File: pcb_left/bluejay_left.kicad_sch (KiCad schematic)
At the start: 0 parts

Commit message: Start building left pcb
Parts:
- added C1, C2: 22p, symbol Device:C_Small
- added U1: ATmega328P-PU, Package_DIP_AKL:DIP-28_W7.62mm_Socket, symbol BlueJaySymbolLibrary:ATmega328P-PU
- added Y1: 16MHz, symbol BlueJaySymbolLibrary:Device_Crystal_Small
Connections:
- new net: C1.1, U1.9 (XTAL1/PB6), Y1.2
- new net: C2.1, U1.10 (XTAL2/PB7), Y1.1
- new net GND: C1.2, C2.2, U1.22 (GND), U1.8 (GND)
- new net VCC: U1.20 (AVCC), U1.7 (VCC)
- no-connect marks 0 -> 1
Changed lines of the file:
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@@
 (kicad_sch (version 20211123) (generator eeschema)
   (paper "USLetter")
+  (junction (at 34.29 114.3) (diameter 0) (color 0 0 0 0)
+  )
+  (junction (at 55.88 143.51) (diameter 0) (color 0 0 0 0)
+  )
+  (junction (at 55.88 138.43) (diameter 0) (color 0 0 0 0)
+  )
+  (junction (at 73.66 146.05) (diameter 0) (color 0 0 0 0)
+  )
+  (no_connect (at 19.05 124.46))
+  (wire (pts (xy 55.88 138.43) (xy 55.88 135.89))
+    (stroke (width 0) (type default) (color 0 0 0 0))
+  )
+  (wire (pts (xy 49.53 138.43) (xy 49.53 139.7))
+    (stroke (width 0) (type default) (color 0 0 0 0))
+  )
+  (wire (pts (xy 73.66 135.89) (xy 73.66 146.05))
+    (stroke (width 0) (type default) (color 0 0 0 0))
+  )
+  (wire (pts (xy 36.83 114.3) (xy 34.29 114.3))
+    (stroke (width 0) (type default) (color 0 0 0 0))
+  )
+  (wire (pts (xy 67.31 135.89) (xy 73.66 135.89))
+    (stroke (width 0) (type default) (color 0 0 0 0))
+  )
+  (wire (pts (xy 55.88 138.43) (xy 49.53 138.43))
+    (stroke (width 0) (type default) (color 0 0 0 0))
+  )
+  (wire (pts (xy 34.29 110.49) (xy 34.29 114.3))
+    (stroke (width 0) (type default) (color 0 0 0 0))
+  )
+  (wire (pts (xy 55.88 143.51) (xy 49.53 143.51))
+    (stroke (width 0) (type default) (color 0 0 0 0))
+  )
+  (wire (pts (xy 36.83 116.84) (xy 36.83 114.3))
+    (stroke (width 0) (type default) (color 0 0 0 0))
+  )
+  (wire (pts (xy 34.29 193.04) (xy 34.29 196.85))
+    (stroke (width 0) (type default) (color 0 0 0 0))
+  )
+  (wire (pts (xy 55.88 135.89) (xy 62.23 135.89))
+    (stroke (width 0) (type default) (color 0 0 0 0))
+  )
+  (wire (pts (xy 34.29 114.3) (xy 34.29 116.84))
+    (stroke (width 0) (type default) (color 0 0 0 0))
+  )
+  (wire (pts (xy 49.53 143.51) (xy 49.53 142.24))
+    (stroke (width 0) (type default) (color 0 0 0 0))
+  )
+  (wire (pts (xy 55.88 143.51) (xy 55.88 146.05))
+    (stroke (width 0) (type default) (color 0 0 0 0))
+  )
+  (wire (pts (xy 67.31 146.05) (xy 73.66 146.05))
+    (stroke (width 0) (type default) (color 0 0 0 0))
+  )
+  (wire (pts (xy 55.88 146.05) (xy 62.23 146.05))
+    (stroke (width 0) (type default) (color 0 0 0 0))
+  )
+  (symbol (lib_id "power:GND") (at 34.29 196.85 0) (unit 1)
+    (in_bom yes) (on_board yes) (fields_autoplaced)
+    (property "Reference" "#PWR?" (id 0) (at 34.29 203.2 0)
+      (effects (font (size 1.27 1.27)) hide)
+    )
+    (property "Value" "GND" (id 1) (at 34.29 201.93 0))
+    (property "Footprint" "" (id 2) (at 34.29 196.85 0)
+      (effects (font (size 1.27 1.27)) hide)
+    )
+    (property "Datasheet" "" (id 3) (at 34.29 196.85 0)
+      (effects (font (size 1.27 1.27)) hide)
+    )
+    (pin "1")
+  )
+  (symbol (lib_id "Device:C_Small") (at 64.77 135.89 90) (unit 1)
+    (in_bom yes) (on_board yes) (fields_autoplaced)
+    (property "Reference" "C1" (id 0) (at 64.7763 129.54 90))
+    (property "Value" "22p" (id 1) (at 64.7763 132.08 90))
+    (property "Footprint" "" (id 2) (at 64.77 135.89 0)
+      (effects (font (size 1.27 1.27)) hide)
+    )
+    (property "Datasheet" "~" (id 3) (at 64.77 135.89 0)
+      (effects (font (size 1.27 1.27)) hide)
+    )
+    (pin "1")
+    (pin "2")
+  )
+  (symbol (lib_id "Device:C_Small") (at 64.77 146.05 90) (unit 1)
+    (in_bom yes) (on_board yes)
+    (property "Reference" "C2" (id 0) (at 64.77 149.86 90))
+    (property "Value" "22p" (id 1) (at 64.77 152.4 90))
+    (property "Footprint" "" (id 2) (at 64.77 146.05 0)
+      (effects (font (size 1.27 1.27)) hide)
+    )
+    (property "Datasheet" "~" (id 3) (at 64.77 146.05 0)
+      (effects (font (size 1.27 1.27)) hide)
+    )
+    (pin "1")
+    (pin "2")
+  )
+  (symbol (lib_id "BlueJaySymbolLibrary:Device_Crystal_Small") (at 55.88 140.97 90) (unit 1)
+    (in_bom yes) (on_board yes)
+    (property "Reference" "Y1" (id 0) (at 57.15 138.43 90)
+      (effects (font (size 1.27 1.27)) (justify right))
+    )
+    (property "Value" "16MHz" (id 1) (at 55.88 144.78 90)
+      (effects (font (size 1.27 1.27)) (justify right))
+    )
+    (property "Footprint" "" (id 2) (at 55.88 140.97 0)
+      (effects (font (size 1.27 1.27)) hide)
+    )
+    (property "Datasheet" "" (id 3) (at 55.88 140.97 0)
+      (effects (font (size 1.27 1.27)) hide)
+    )
+    (pin "1")
+    (pin "2")
+  )
+  (symbol (lib_id "power:VCC") (at 34.29 110.49 0) (unit 1)
+    (in_bom yes) (on_board yes) (fields_autoplaced)
+    (property "Reference" "#PWR?" (id 0) (at 34.29 114.3 0)
+      (effects (font (size 1.27 1.27)) hide)
+    )
+    (property "Value" "VCC" (id 1) (at 34.29 105.41 0))
+    (property "Footprint" "" (id 2) (at 34.29 110.49 0)
+      (effects (font (size 1.27 1.27)) hide)
+    )
+    (property "Datasheet" "" (id 3) (at 34.29 110.49 0)
+      (effects (font (size 1.27 1.27)) hide)
+    )
+    (pin "1")
+  )
+  (symbol (lib_id "power:GND") (at 73.66 146.05 0) (unit 1)
+    (in_bom yes) (on_board yes) (fields_autoplaced)
+    (property "Reference" "#PWR?" (id 0) (at 73.66 152.4 0)
+      (effects (font (size 1.27 1.27)) hide)
+    )
+    (property "Value" "GND" (id 1) (at 73.66 151.13 0))
+    (property "Footprint" "" (id 2) (at 73.66 146.05 0)
+      (effects (font (size 1.27 1.27)) hide)
+    )
+    (property "Datasheet" "" (id 3) (at 73.66 146.05 0)
+      (effects (font (size 1.27 1.27)) hide)
+    )
+    (pin "1")
+  )
+  (symbol (lib_id "BlueJaySymbolLibrary:ATmega328P-PU") (at 34.29 154.94 0) (unit 1)
+    (in_bom yes) (on_board yes)
+    (property "Reference" "U1" (id 0) (at 21.59 114.3 0))
+    (property "Value" "ATmega328P-PU" (id 1) (at 21.59 116.84 0))
+    (property "Footprint" "Package_DIP_AKL:DIP-28_W7.62mm_Socket" (id 2) (at 34.29 154.94 0)
+      (effects (font (size 1.27 1.27) italic) hide)
+    )
+    (property "Datasheet" "" (id 3) (at 34.29 154.94 0)
+      (effects (font (size 1.27 1.27)) hide)
+    )
+    (pin "1")
+    (pin "10")
+    (pin "11")
+    (pin "12")
+    (pin "13")
+    (pin "14")
+    (pin "15")
+    (pin "16")
+    (pin "17")
+    (pin "18")
+    (pin "19")
+    (pin "2")
+    (pin "20")
+    (pin "21")
+    (pin "22")
+    (pin "23")
+    (pin "24")
+    (pin "25")
+    (pin "26")
+    (pin "27")
+    (pin "28")
+    (pin "3")
+    (pin "4")
+    (pin "5")
+    (pin "6")
+    (pin "7")
+    (pin "8")
+    (pin "9")
+  )
   (sheet_instances
     (path "/" (page "1"))
   )
+  (symbol_instances
+    (path "/35c4581b-ad58-4c6a-b9b5-a7da8d3ffce0"
+      (reference "#PWR?") (unit 1) (value "GND") (footprint "")
+    )
+    (path "/dbad4ed4-d45c-4d59-94e2-f9535f75f8ab"
+      (reference "#PWR?") (unit 1) (value "VCC") (footprint "")
+    )
+    (path "/ef505780-efbb-4972-90a1-9efb3e3977fd"
+      (reference "#PWR?") (unit 1) (value "GND") (footprint "")
+    )
+    (path "/709a6874-5923-446e-9322-a60e23d13f71"
+      (reference "C1") (unit 1) (value "22p") (footprint "")
+    )
+    (path "/a0c76107-1620-4d05-9cfd-c1cc933ae005"
+      (reference "C2") (unit 1) (value "22p") (footprint "")
+    )
+    (path "/f0419025-a2cc-429c-b657-aae4c613bf31"
+      (reference "U1") (unit 1) (value "ATmega328P-PU") (footprint "Package_DIP_AKL:DIP-28_W7.62mm_Socket")
+    )
+    (path "/a4afee0d-8e42-4a5d-aac7-862e4657a136"
+      (reference "Y1") (unit 1) (value "16MHz") (footprint "")
+    )
+  )
 )

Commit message: More work on left hand schematic
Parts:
- added C3: 4.7u, symbol BlueJaySymbolLibrary:Device_CP1_Small
- added C4, C5: 100n, symbol BlueJaySymbolLibrary:C_Small
- added D1A: 1N4148, Diode_THT_AKL:D_DO-35_SOD27_P7.62mm_Horizontal, symbol Diode_AKL:1N4148
- added DZ1, DZ2: 3.6V, Diode_THT_AKL:D_DO-35_SOD27_P7.62mm_Horizontal_Zener, symbol Diode_Zener_AKL:BZX79-C3V6
- added F1: 100mA, symbol BlueJaySymbolLibrary:Device_Polyfuse_Small
- added J1: SJ-43514, CUI_SJ-43514, symbol BlueJaySymbolLibrary:SJ-43514
- added PB1: RESET, symbol BlueJaySymbolLibrary:Switch_SW_Push
- added PB2: BOOT, symbol BlueJaySymbolLibrary:Switch_SW_Push
- added R1: 1.5k, symbol BlueJaySymbolLibrary:Device_R_Small
- added R2, R3: 75R, symbol BlueJaySymbolLibrary:Device_R_Small
- added R4: 10k, symbol BlueJaySymbolLibrary:Device_R_Small
- added SW1A: KEYSW, symbol BlueJaySymbolLibrary:Switch_SW_Push
- added USB1: USB_B_Mini, symbol Connector:USB_B_Mini
- C1, C2: symbol Device:C_Small -> BlueJaySymbolLibrary:C_Small
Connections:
- net GND: now also C3.2, C4.2, C5.2, DZ1.2 (A), DZ2.2 (A), J1.1, PB1.2, PB2.2, USB1.5 (GND), USB1.6 (Shield)
- net VCC: now also C3.1, C4.1, C5.1, F1.1, J1.2, R1.2, R4.1
- net at U1.1 (~{RESET}/PC6): now also PB1.1, R4.2
- net at U1.2 (PD0): now also PB2.1
- net i2c_SDA: now reaches U1.27 (PC4)
- net i2c_SDA: now also J1.4
- net i2c_SCL: now reaches U1.28 (PC5)
- net i2c_SCL: now also J1.3
- net USB_D+: now reaches U1.4 (PD2)
- net USB_D+: now also R3.1
- net USB_D-: now reaches U1.5 (PD3)
- net USB_D-: now also R2.1
- new net: DZ1.1 (K), R1.1, R2.2, USB1.2 (D-)
- new net: DZ2.1 (K), R3.2, USB1.3 (D+)
- new net: F1.2, USB1.1 (VBUS)
- no-connect marks 1 -> 2
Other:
- moved on the sheet: C1, C2

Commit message: Further progress with left hand schematic
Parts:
- added D1B, D2A, D2A?, D3A, D3A?, D4A, D4A?, D5A, D5A?: 1N4148, Diode_THT_AKL:D_DO-35_SOD27_P7.62mm_Horizontal, symbol Diode_AKL:1N4148
- added SW1B, SW2A, SW2A?, SW3A, SW3A?, SW4A, SW4A?, SW5A, SW5A?: KEYSW, symbol BlueJaySymbolLibrary:Switch_SW_Push
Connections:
- net colA: now reaches D1A.1 (K)
- net colA: now also D2A.1 (K), D3A.1 (K), D4A.1 (K), D5A.1 (K)
- net at D1A.2 (A): now also SW1A.1
- net row1: now reaches SW1A.2
- net row1: now also SW1B.2
- new net: D4A.2 (A), SW4A.1
- new net: D2A.2 (A), SW2A.1
- new net: D3A?.2 (A), SW3A?.1
- new net: D2A?.2 (A), SW2A?.1
- new net: D4A?.2 (A), SW4A?.1
- new net: D1B.2 (A), SW1B.1
- new net: D5A?.2 (A), SW5A?.1
- new net: D3A.2 (A), SW3A.1
- new net: D5A.2 (A), SW5A.1
- new net colB: D1B.1 (K), D2A?.1 (K), D3A?.1 (K), D4A?.1 (K), D5A?.1 (K)
- new net row2: SW2A.2, SW2A?.2
- new net row3: SW3A.2, SW3A?.2
- new net row4: SW4A.2, SW4A?.2
- new net row5: SW5A.2, SW5A?.2
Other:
- moved on the sheet: D1A, SW1A

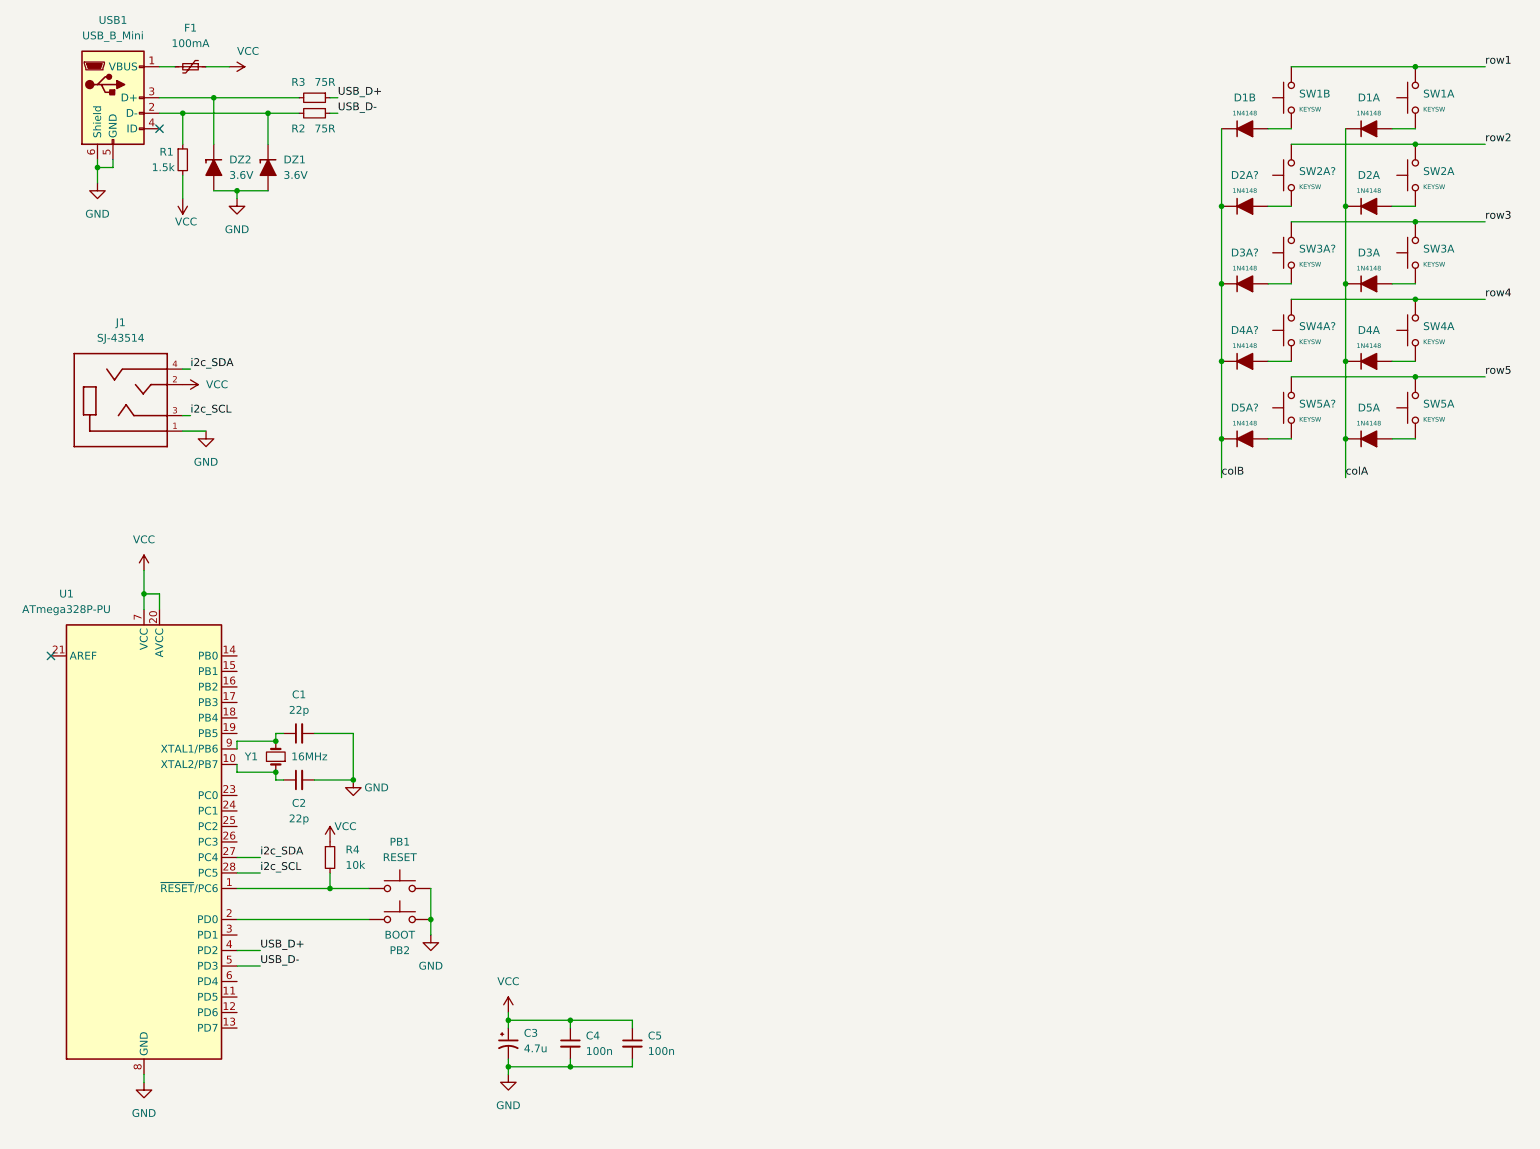
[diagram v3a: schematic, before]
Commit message: Update bluejay_left.kicad_sch
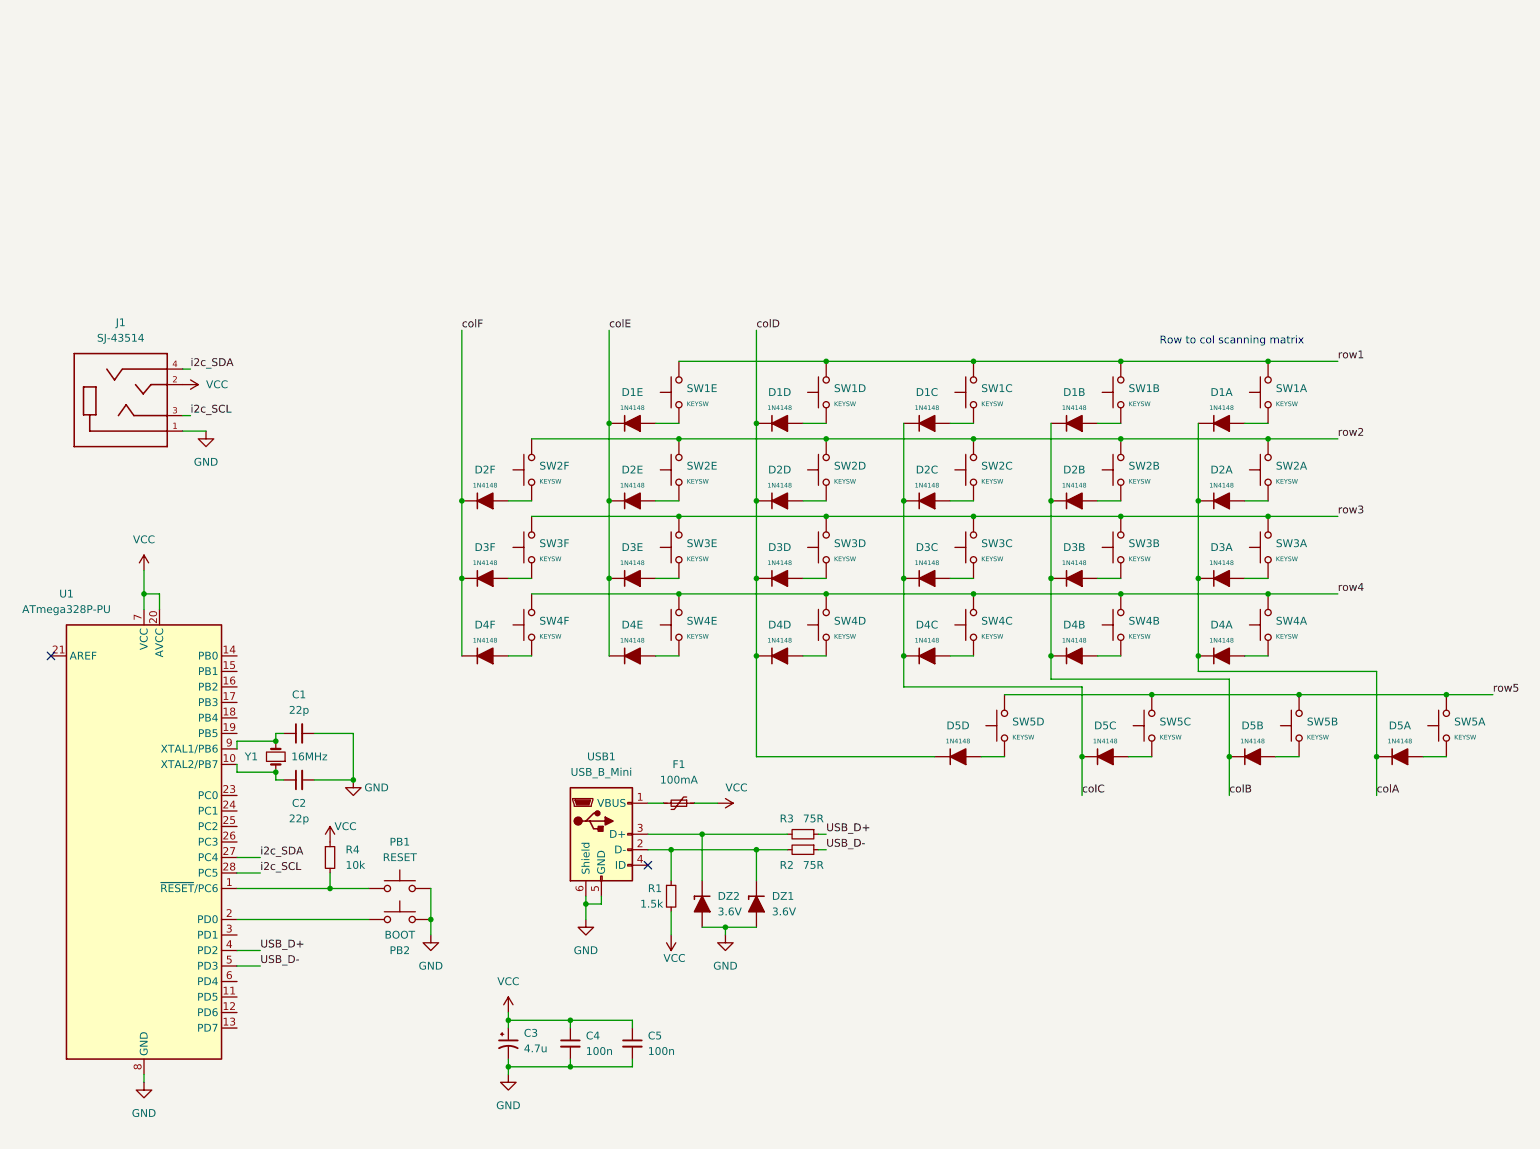
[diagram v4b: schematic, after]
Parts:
- added D1C, D1D, D1E, D2C, D2D, D2E, D2F, D3C, D3D, D3E, D3F, D4C, D4D, D4E, D4F, D5C, D5D: 1N4148, Diode_THT_AKL:D_DO-35_SOD27_P7.62mm_Horizontal, symbol Diode_AKL:1N4148
- added SW1C, SW1D, SW1E, SW2C, SW2D, SW2E, SW2F, SW3C, SW3D, SW3E, SW3F, SW4C, SW4D, SW4E, SW4F, SW5C, SW5D: KEYSW, symbol BlueJaySymbolLibrary:Switch_SW_Push
- gave numbers to parts that had none: 8
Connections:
- net row1: now also SW1C.2, SW1D.2, SW1E.2
- net row2: now also SW2C.2, SW2D.2, SW2E.2, SW2F.2
- net row3: now also SW3C.2, SW3D.2, SW3E.2, SW3F.2
- net row4: now also SW4C.2, SW4D.2, SW4E.2, SW4F.2
- net row5: now also SW5C.2, SW5D.2
- new net: D4E.2 (A), SW4E.1
- new net: D4C.2 (A), SW4C.1
- new net: D1D.2 (A), SW1D.1
- new net: D2F.2 (A), SW2F.1
- new net: D1C.2 (A), SW1C.1
- new net: D2C.2 (A), SW2C.1
- new net: D3E.2 (A), SW3E.1
- new net: D3D.2 (A), SW3D.1
- new net: D2D.2 (A), SW2D.1
- new net: D2E.2 (A), SW2E.1
- new net: D3F.2 (A), SW3F.1
- new net: D5D.2 (A), SW5D.1
- new net: D3C.2 (A), SW3C.1
- new net: D4D.2 (A), SW4D.1
- new net: D4F.2 (A), SW4F.1
- new net: D1E.2 (A), SW1E.1
- new net: D5C.2 (A), SW5C.1
- new net colC: D1C.1 (K), D2C.1 (K), D3C.1 (K), D4C.1 (K), D5C.1 (K)
- new net colD: D1D.1 (K), D2D.1 (K), D3D.1 (K), D4D.1 (K), D5D.1 (K)
- new net colE: D1E.1 (K), D2E.1 (K), D3E.1 (K), D4E.1 (K)
- new net colF: D2F.1 (K), D3F.1 (K), D4F.1 (K)
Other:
- note added: "Row to col scanning matrix"
- moved on the sheet: D1A, D1B, D2A, D2B, D3A, D3B, D4A, D4B, D5A, D5B, DZ1, DZ2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

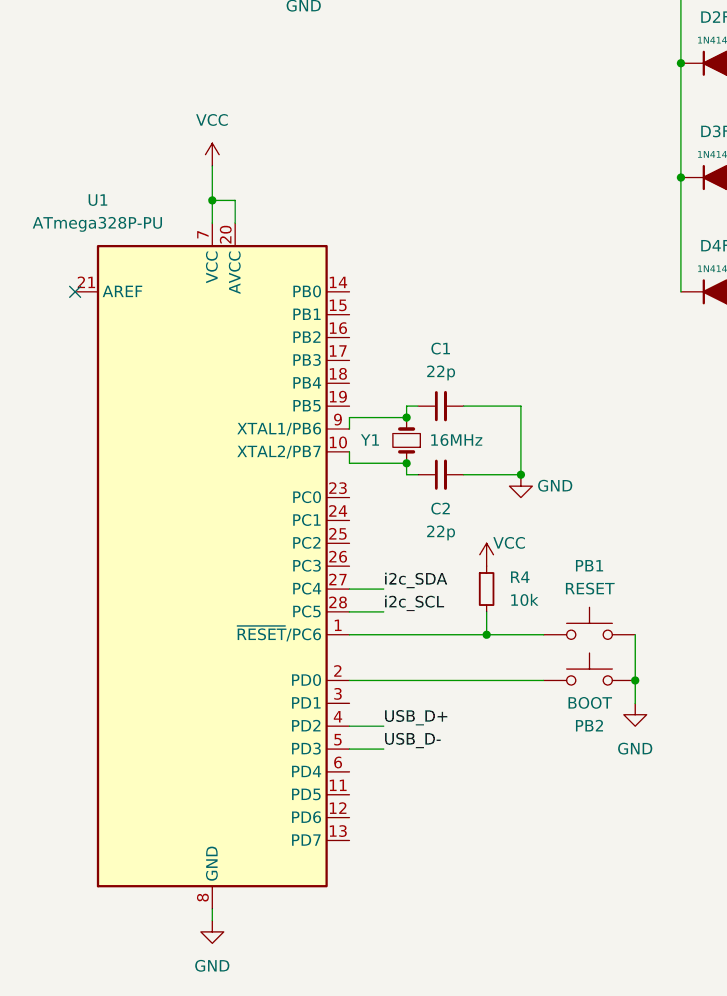
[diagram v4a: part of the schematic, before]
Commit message: Complete left hand schematic
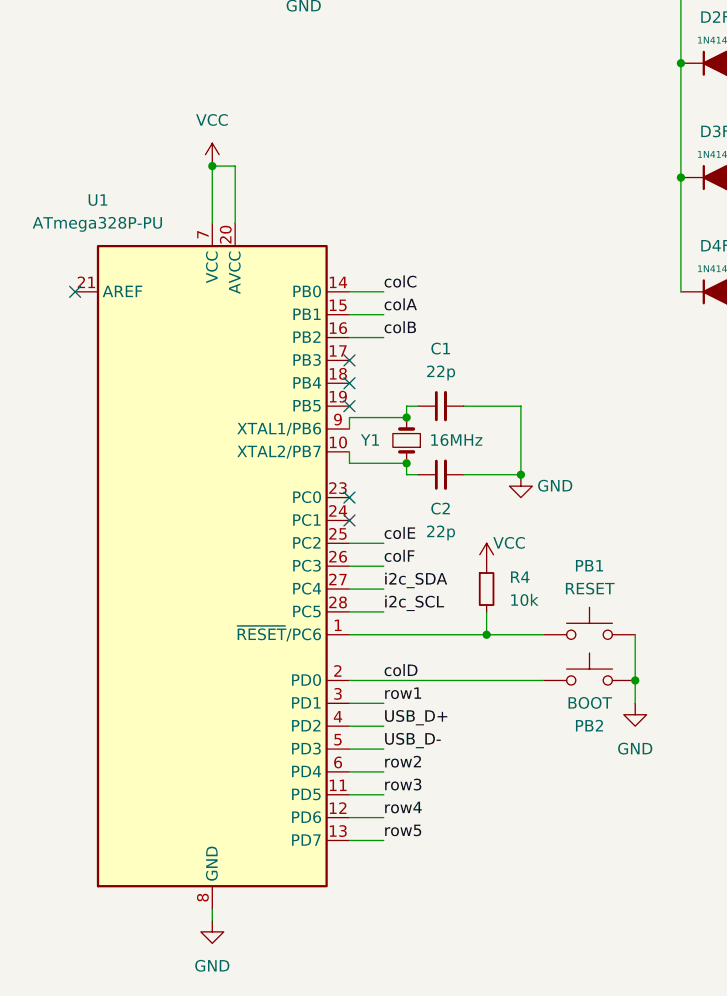
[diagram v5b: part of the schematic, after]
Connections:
- net colA: now also U1.15 (PB1)
- net colB: now also U1.16 (PB2)
- net colC: now also U1.14 (PB0)
- net colD: now also PB2.1, U1.2 (PD0)
- net colE: now also U1.25 (PC2)
- net colF: now also U1.26 (PC3)
- net row1: now also U1.3 (PD1)
- net row2: now also U1.6 (PD4)
- net row3: now also U1.11 (PD5)
- net row4: now also U1.12 (PD6)
- net row5: now also U1.13 (PD7)
- no-connect marks 2 -> 7
